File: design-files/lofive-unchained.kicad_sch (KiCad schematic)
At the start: 39 parts, among them J1 Conn_01x09, J2 Conn_01x09, J3 USB_C_Receptacle_USB2.0, SW1 SW_Push, SW2 SW_Push, U1 ESP32-C3, U2 W25Q32JVZP, U3 TLV62569DRL, Y1 40Mhz

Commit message: Switch to HRO USB connector
Available at LCSC.
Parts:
- J3: footprint Connector_USB:USB_C_Receptacle_Palconn_UTC16-G -> Connector_USB:USB_C_Receptacle_HRO_TYPE-C-31-M-12
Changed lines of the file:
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@@
       (effects (font (size 1.27 1.27)) (justify right))
     )
-    (property "Footprint" "Connector_USB:USB_C_Receptacle_Palconn_UTC16-G" (id 2) (at 236.22 55.88 0)
+    (property "Footprint" "Connector_USB:USB_C_Receptacle_HRO_TYPE-C-31-M-12" (id 2) (at 236.22 55.88 0)
       (effects (font (size 1.27 1.27)) hide)
     )
@@
     )
     (path "/bef403e8-2c26-4719-93d2-347defeb2969"
-      (reference "J3") (unit 1) (value "USB_C_Receptacle_USB2.0") (footprint "Connector_USB:USB_C_Receptacle_Palconn_UTC16-G")
+      (reference "J3") (unit 1) (value "USB_C_Receptacle_USB2.0") (footprint "Connector_USB:USB_C_Receptacle_HRO_TYPE-C-31-M-12")
     )
     (path "/fc19b7c5-e4c2-4287-9459-78ed575099e0"

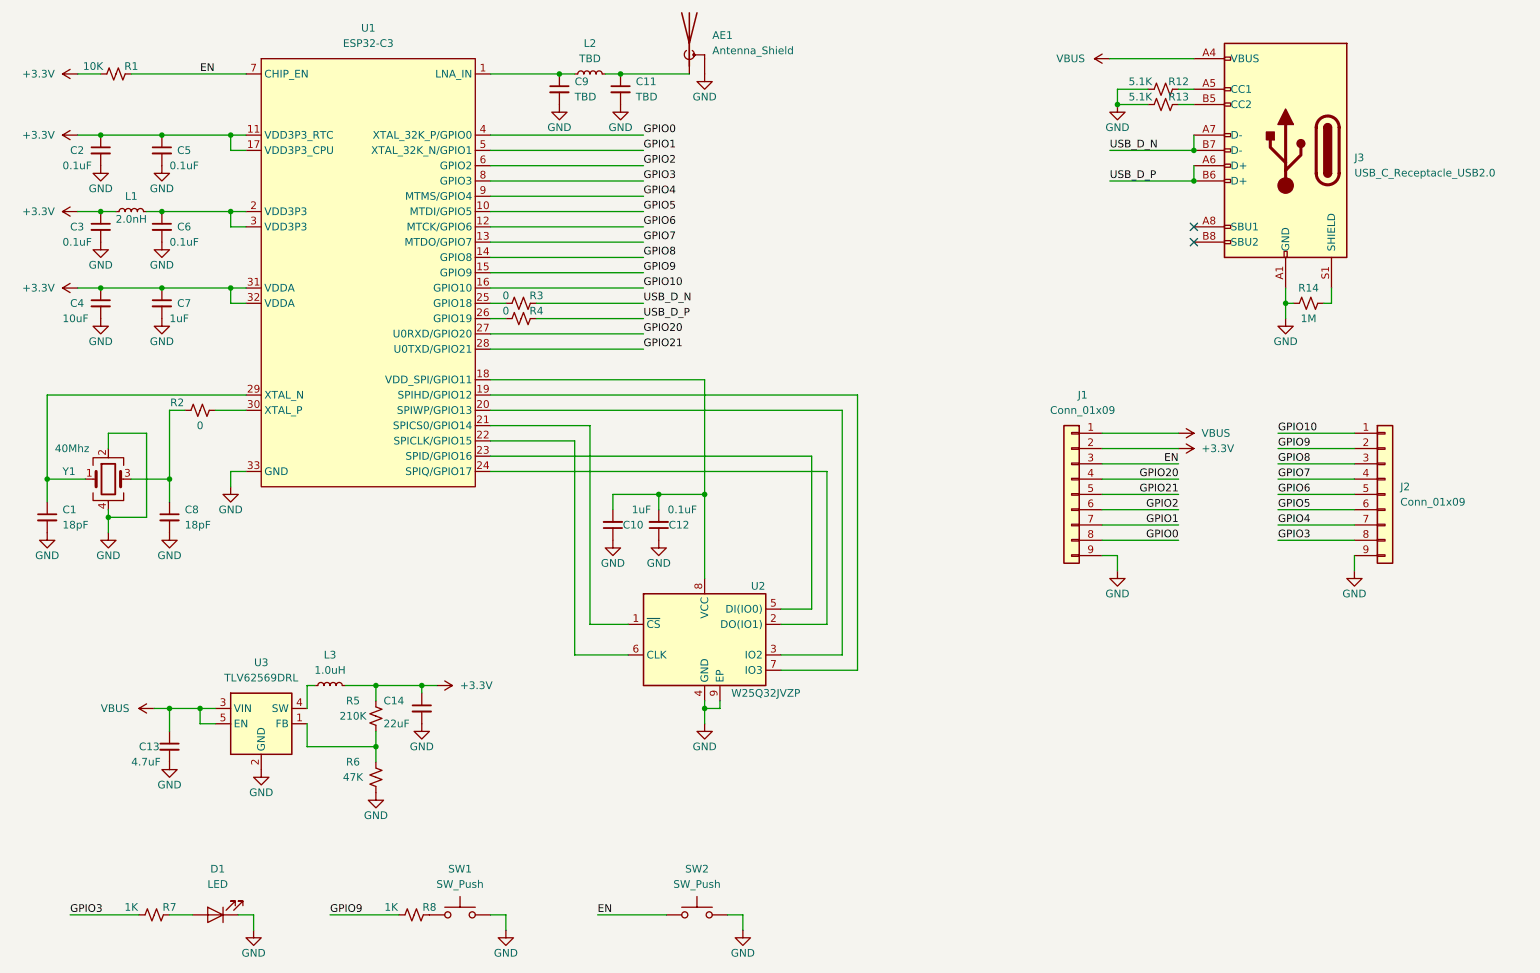
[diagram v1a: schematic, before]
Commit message: Add consummate vias and plot
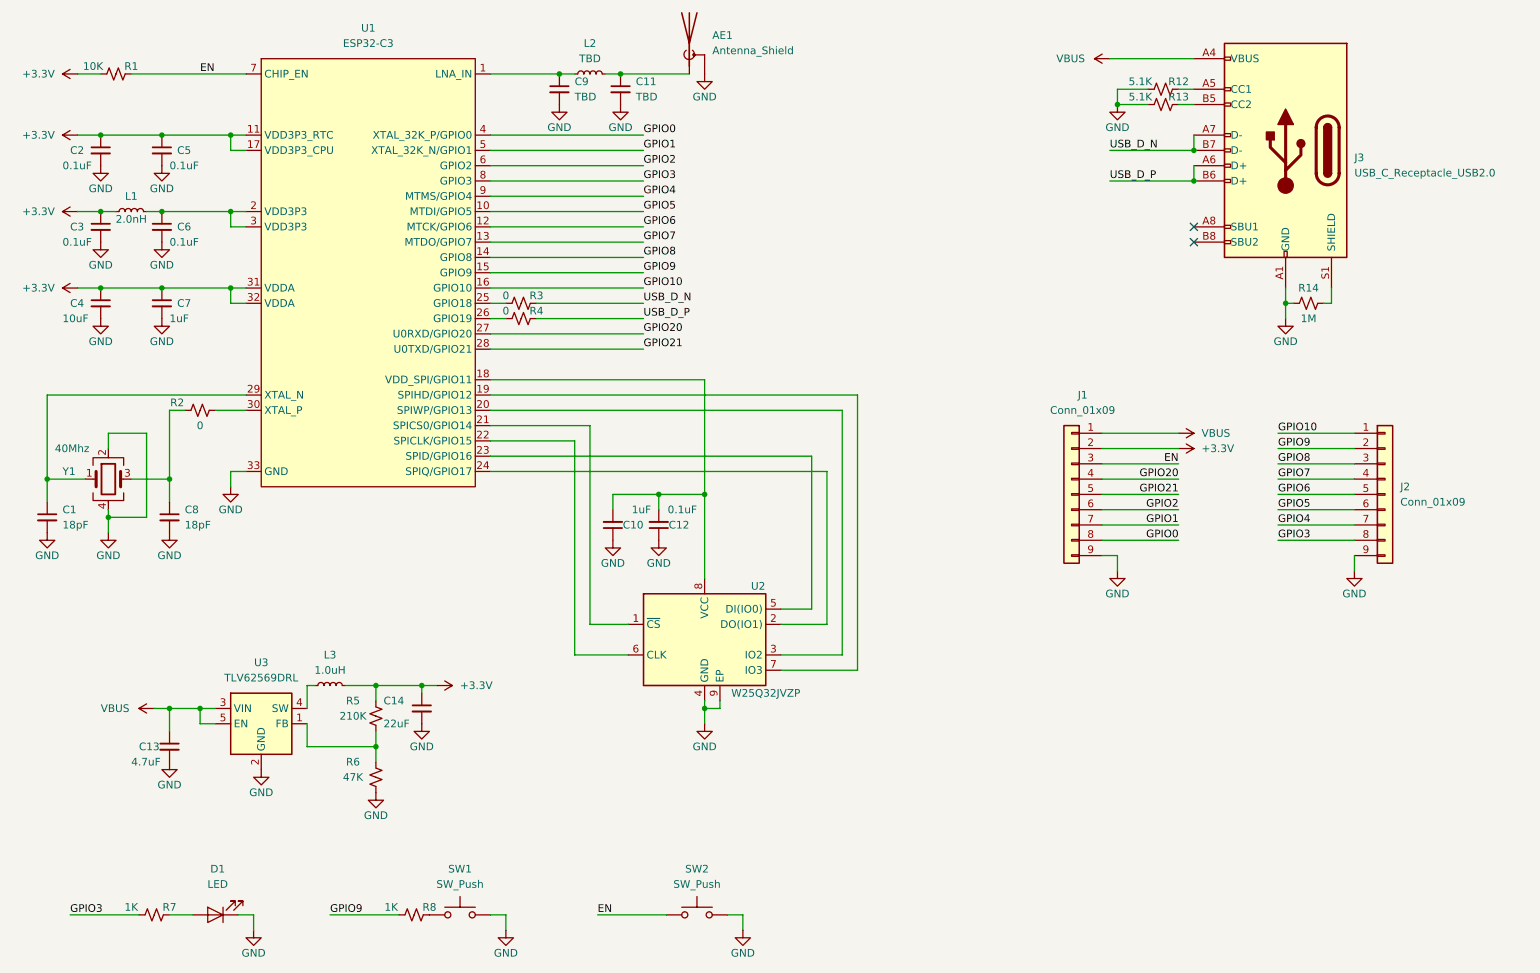
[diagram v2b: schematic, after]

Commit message: Switch to 3.3V LDO instead of switcher
Signed-off-by: Michael Welling <mwelling79@gmail.com>
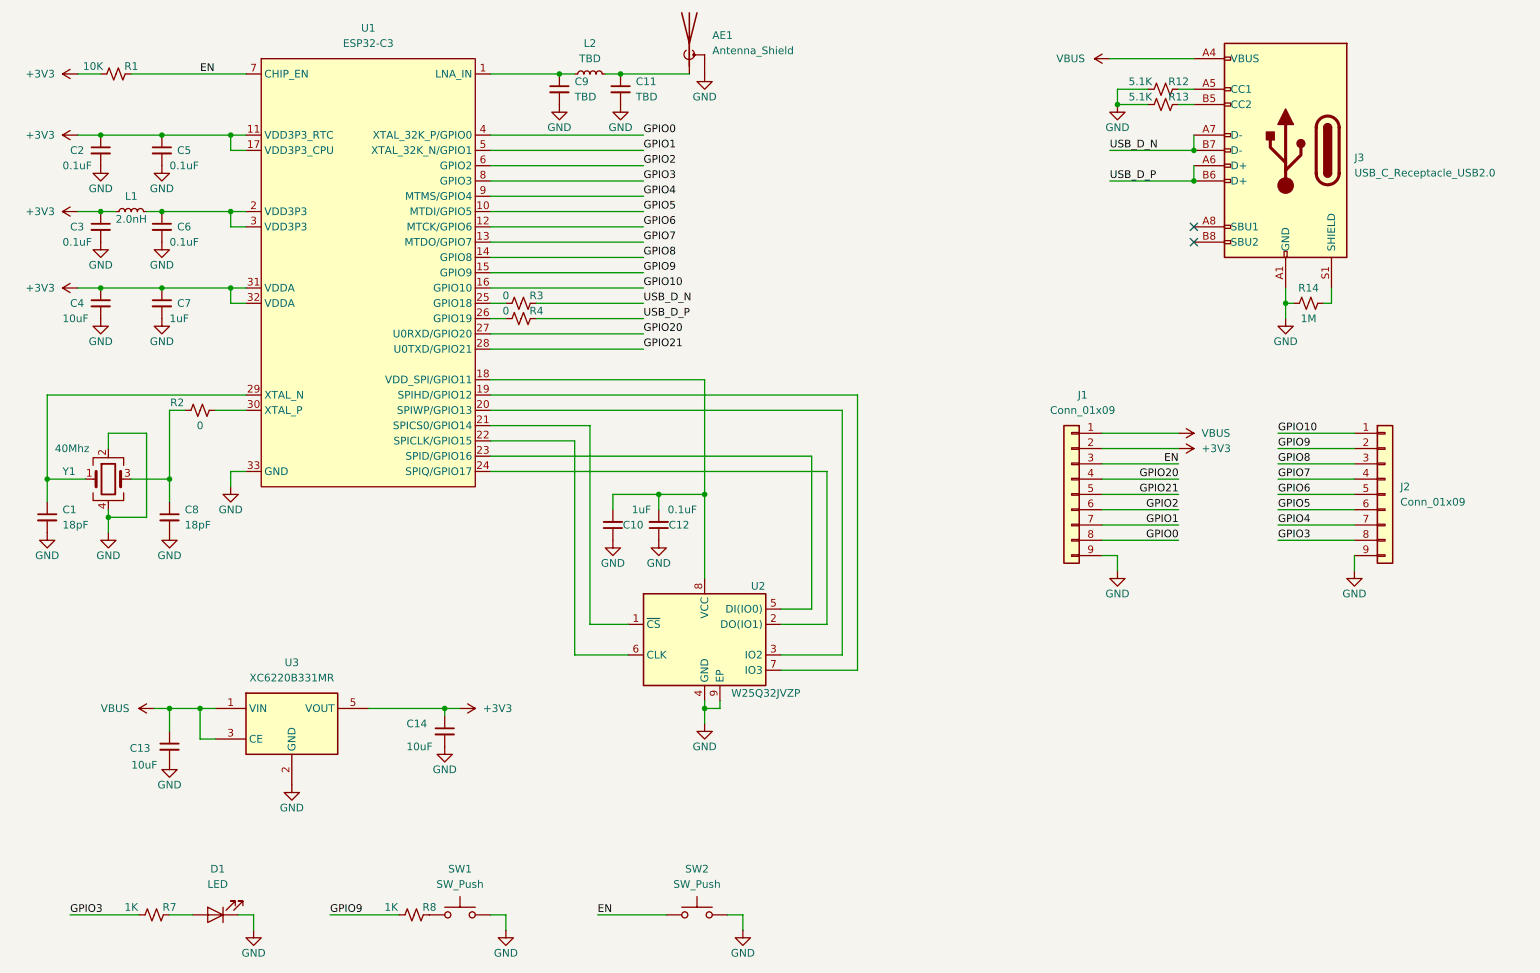
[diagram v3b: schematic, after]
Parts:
- removed L3: 1.0uH, Inductor_SMD:L_0805_2012Metric, symbol Device:L_Small
- removed R5: 210K, Resistor_SMD:R_0402_1005Metric, symbol Device:R_Small_US
- removed R6: 47K, Resistor_SMD:R_0402_1005Metric, symbol Device:R_Small_US
- removed U3: TLV62569DRL, Package_TO_SOT_SMD:SOT-563, symbol Regulator_Switching:TLV62569DRL
- added U3: XC6220B331MR, Package_TO_SOT_SMD:SOT-23-5, symbol Regulator_Linear:XC6220B331MR
- C13: value 4.7uF -> 10uF
- C14: value 22uF -> 10uF
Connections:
- net +3V3: now also U3.5 (VOUT)
- net GND: now also U3.2 (GND)
- net VBUS: now also U3.1 (VIN), U3.3 (CE)
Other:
- moved on the sheet: C14
